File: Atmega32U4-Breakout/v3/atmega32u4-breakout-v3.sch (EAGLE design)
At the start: 54 parts, among them U1 ATMEGA32U4

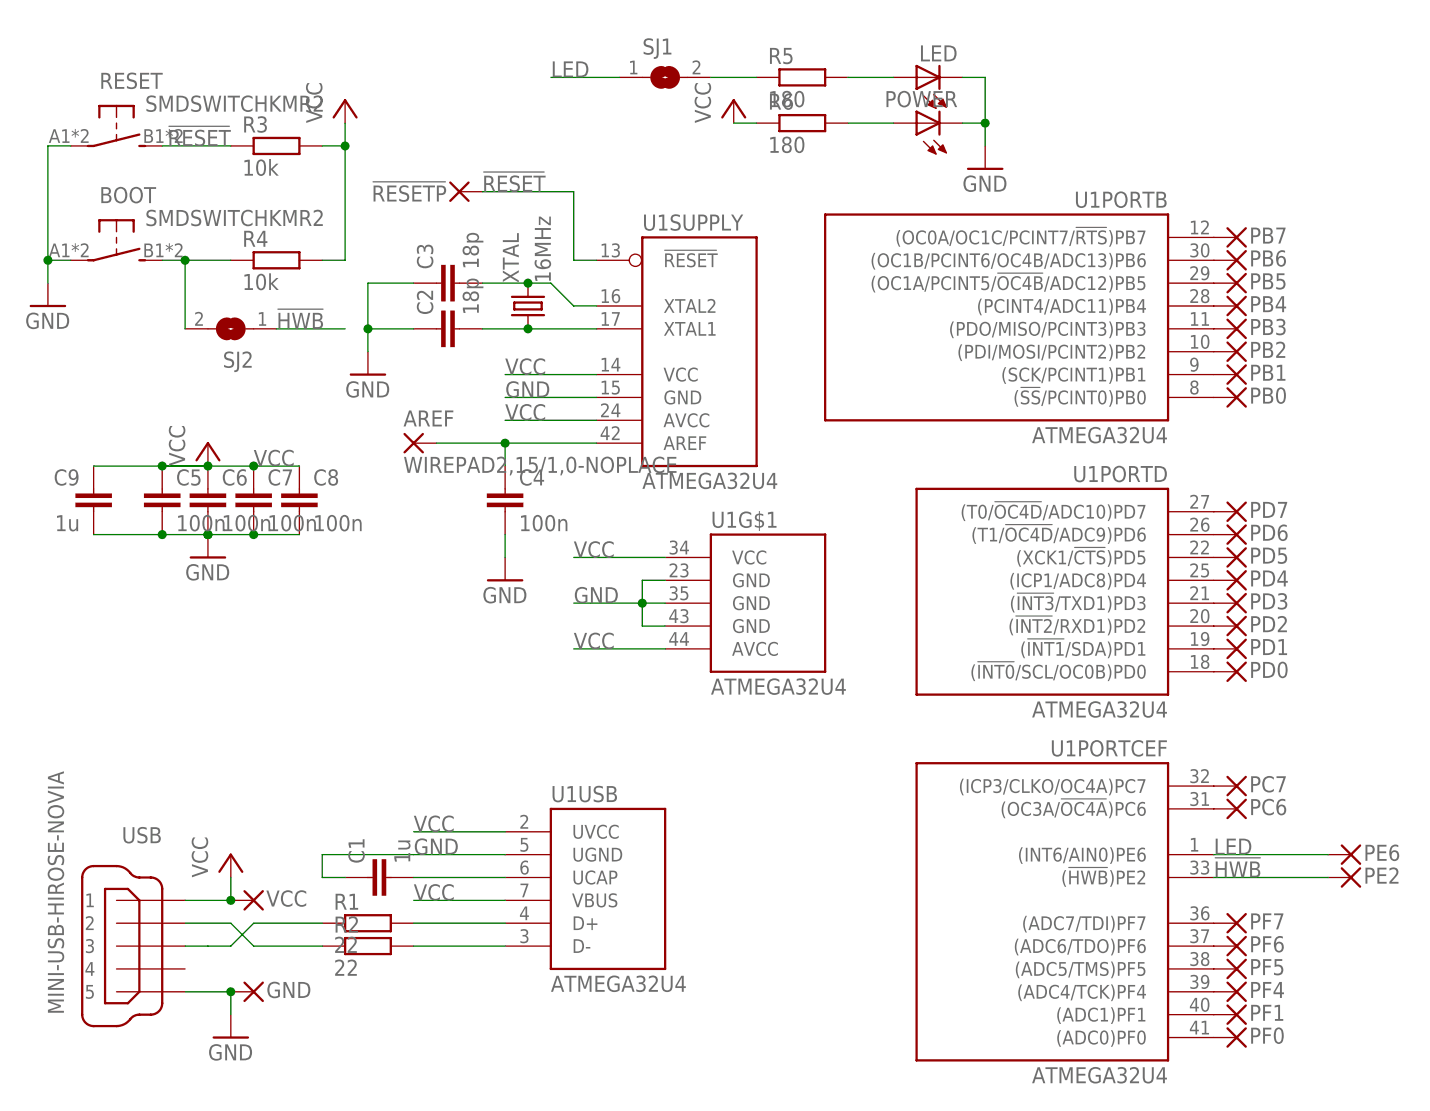
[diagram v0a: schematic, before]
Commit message: - Add silkscreen line between LED resistors so their orientation becomes   more clear. - Change green LED resistor to 150R - Change input filter cap to 0805 4.7uF - Match BOM
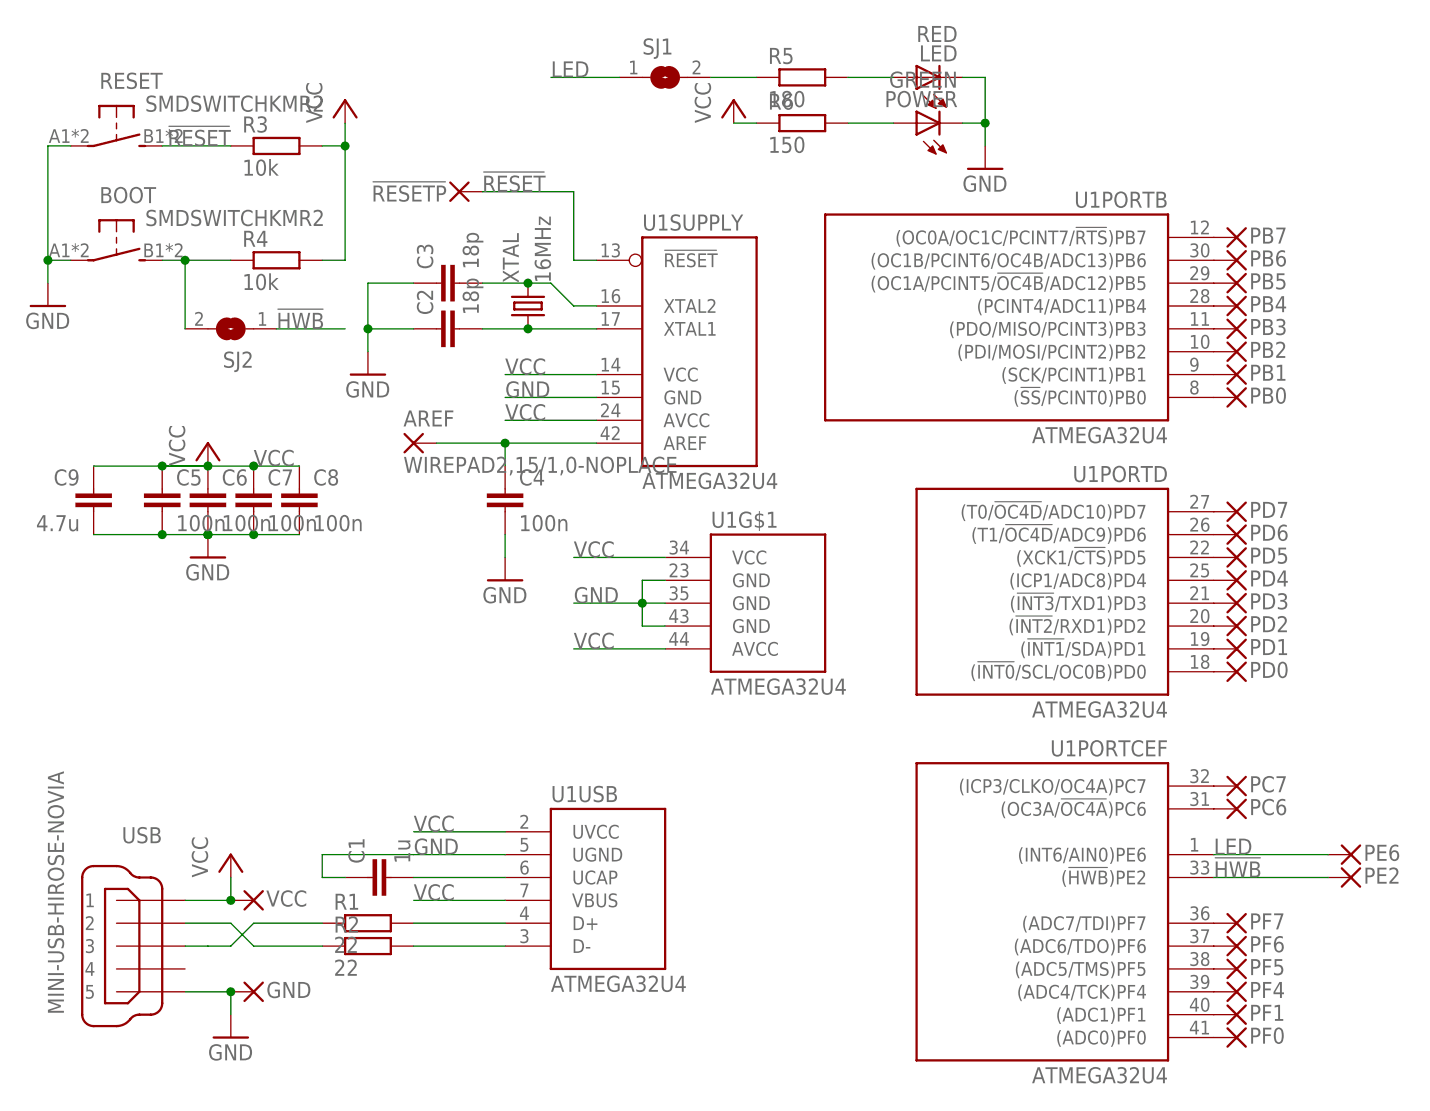
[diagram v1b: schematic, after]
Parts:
- C9: value 1u -> 4.7u; device rcl:C-EUC0603K -> rcl:C-EUC0805K
- LED: value (none) -> RED
- POWER: value (none) -> GREEN
- R6: value 180 -> 150
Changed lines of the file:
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@@
 <?xml version="1.0" encoding="utf-8"?>
 <!DOCTYPE eagle SYSTEM "eagle.dtd">
-<eagle version="6.0">
+<eagle version="6.1">
 <drawing>
 <settings>
@@
 <grid distance="0.1" unitdist="inch" unit="inch" style="lines" multiple="1" display="no" altdistance="0.01" altunitdist="inch" altunit="inch"/>
 <layers>
-<layer number="1" name="Top" color="4" fill="1" visible="yes" active="no"/>
-<layer number="16" name="Bottom" color="1" fill="1" visible="yes" active="no"/>
-<layer number="17" name="Pads" color="2" fill="1" visible="yes" active="no"/>
-<layer number="18" name="Vias" color="2" fill="1" visible="yes" active="no"/>
-<layer number="19" name="Unrouted" color="6" fill="1" visible="yes" active="no"/>
-<layer number="20" name="Dimension" color="15" fill="1" visible="yes" active="no"/>
-<layer number="21" name="tPlace" color="7" fill="1" visible="yes" active="no"/>
-<layer number="22" name="bPlace" color="7" fill="1" visible="yes" active="no"/>
-<layer number="23" name="tOrigins" color="15" fill="1" visible="yes" active="no"/>
-<layer number="24" name="bOrigins" color="15" fill="1" visible="yes" active="no"/>
-<layer number="25" name="tNames" color="7" fill="1" visible="yes" active="no"/>
-<layer number="26" name="bNames" color="7" fill="1" visible="yes" active="no"/>
-<layer number="27" name="tValues" color="7" fill="1" visible="yes" active="no"/>
-<layer number="28" name="bValues" color="7" fill="1" visible="yes" active="no"/>
+<layer number="1" name="Top" color="4" fill="1" visible="no" active="no"/>
+<layer number="16" name="Bottom" color="1" fill="1" visible="no" active="no"/>
+<layer number="17" name="Pads" color="2" fill="1" visible="no" active="no"/>
+<layer number="18" name="Vias" color="2" fill="1" visible="no" active="no"/>
+<layer number="19" name="Unrouted" color="6" fill="1" visible="no" active="no"/>
+<layer number="20" name="Dimension" color="15" fill="1" visible="no" active="no"/>
+<layer number="21" name="tPlace" color="7" fill="1" visible="no" active="no"/>
+<layer number="22" name="bPlace" color="7" fill="1" visible="no" active="no"/>
+<layer number="23" name="tOrigins" color="15" fill="1" visible="no" active="no"/>
+<layer number="24" name="bOrigins" color="15" fill="1" visible="no" active="no"/>
+<layer number="25" name="tNames" color="7" fill="1" visible="no" active="no"/>
+<layer number="26" name="bNames" color="7" fill="1" visible="no" active="no"/>
+<layer number="27" name="tValues" color="7" fill="1" visible="no" active="no"/>
+<layer number="28" name="bValues" color="7" fill="1" visible="no" active="no"/>
 <layer number="29" name="tStop" color="7" fill="3" visible="no" active="no"/>
 <layer number="30" name="bStop" color="7" fill="6" visible="no" active="no"/>
@@
 <layer number="35" name="tGlue" color="7" fill="4" visible="no" active="no"/>
 <layer number="36" name="bGlue" color="7" fill="5" visible="no" active="no"/>
-<layer number="37" name="tTest" color="7" fill="1" visible="yes" active="no"/>
-<layer number="38" name="bTest" color="7" fill="1" visible="yes" active="no"/>
+<layer number="37" name="tTest" color="7" fill="1" visible="no" active="no"/>
+<layer number="38" name="bTest" color="7" fill="1" visible="no" active="no"/>
 <layer number="39" name="tKeepout" color="4" fill="11" visible="no" active="no"/>
 <layer number="40" name="bKeepout" color="1" fill="11" visible="no" active="no"/>
@@
 <layer number="44" name="Drills" color="7" fill="1" visible="no" active="no"/>
 <layer number="45" name="Holes" color="7" fill="1" visible="no" active="no"/>
-<layer number="46" name="Milling" color="3" fill="1" visible="yes" active="no"/>
-<layer number="47" name="Measures" color="7" fill="1" visible="yes" active="no"/>
-<layer number="48" name="Document" color="7" fill="1" visible="yes" active="no"/>
-<layer number="49" name="Reference" color="7" fill="1" visible="yes" active="no"/>
-<layer number="50" name="dxf" color="7" fill="1" visible="yes" active="no"/>
-<layer number="51" name="tDocu" color="7" fill="1" visible="yes" active="no"/>
-<layer number="52" name="bDocu" color="7" fill="1" visible="yes" active="no"/>
-<layer number="53" name="tGND_GNDA" color="7" fill="9" visible="yes" active="no"/>
-<layer number="54" name="bGND_GNDA" color="1" fill="9" visible="yes" active="no"/>
-<layer number="56" name="wert" color="7" fill="1" visible="yes" active="no"/>
+<layer number="46" name="Milling" color="3" fill="1" visible="no" active="no"/>
+<layer number="47" name="Measures" color="7" fill="1" visible="no" active="no"/>
+<layer number="48" name="Document" color="7" fill="1" visible="no" active="no"/>
+<layer number="49" name="Reference" color="7" fill="1" visible="no" active="no"/>
+<layer number="50" name="dxf" color="7" fill="1" visible="no" active="no"/>
+<layer number="51" name="tDocu" color="7" fill="1" visible="no" active="no"/>
+<layer number="52" name="bDocu" color="7" fill="1" visible="no" active="no"/>
+<layer number="53" name="tGND_GNDA" color="7" fill="9" visible="no" active="no"/>
+<layer number="54" name="bGND_GNDA" color="1" fill="9" visible="no" active="no"/>
+<layer number="56" name="wert" color="7" fill="1" visible="no" active="no"/>
 <layer number="91" name="Nets" color="2" fill="1" visible="yes" active="yes"/>
 <layer number="92" name="Busses" color="1" fill="1" visible="yes" active="yes"/>
@@
 <part name="GND4" library="supply1" deviceset="GND" device=""/>
 <part name="P+2" library="supply1" deviceset="VCC" device=""/>
-<part name="C9" library="rcl" deviceset="C-EU" device="C0603K" value="1u"/>
+<part name="C9" library="rcl" deviceset="C-EU" device="C0805K" value="4.7u"/>
 <part name="PB0" library="jocki" deviceset="WIREPAD" device="2,15/1,0-NOPLACE"/>
 <part name="PB1" library="jocki" deviceset="WIREPAD" device="2,15/1,0-NOPLACE"/>
@@
 <part name="VCC" library="jocki" deviceset="WIREPAD" device="2,15/1,0-NOPLACE"/>
 <part name="R5" library="rcl" deviceset="R-EU_" device="R0603" value="180"/>
-<part name="R6" library="rcl" deviceset="R-EU_" device="R0603" value="180"/>
+<part name="R6" library="rcl" deviceset="R-EU_" device="R0603" value="150"/>
 <part name="SJ1" library="jumper" deviceset="SJ" device=""/>
-<part name="LED" library="led" deviceset="LED" device="CHIPLED_0805"/>
-<part name="POWER" library="led" deviceset="LED" device="CHIPLED_0805"/>
+<part name="LED" library="led" deviceset="LED" device="CHIPLED_0805" value="RED"/>
+<part name="POWER" library="led" deviceset="LED" device="CHIPLED_0805" value="GREEN"/>
 <part name="GND8" library="supply1" deviceset="GND" device=""/>
 <part name="P+4" library="supply1" deviceset="VCC" device=""/>

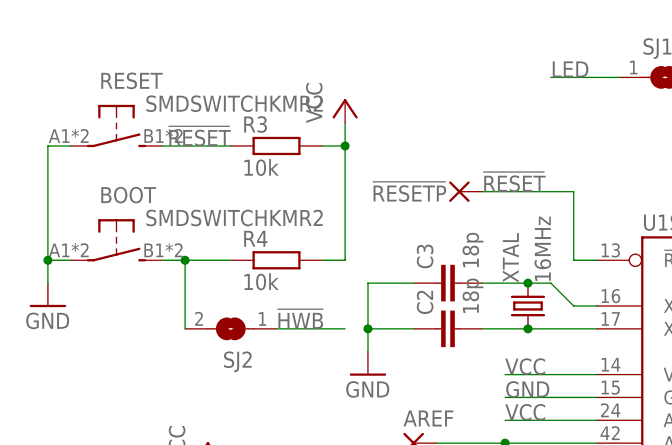
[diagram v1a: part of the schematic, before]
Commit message: Straighten a few bits of the layout, adapt to switches with ground pin. Also, match BOM.
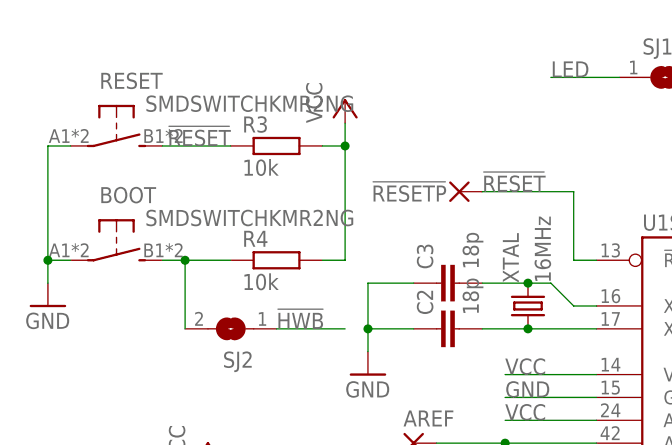
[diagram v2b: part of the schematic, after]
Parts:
- BOOT, RESET: value SMDSWITCHKMR2 -> SMDSWITCHKMR2NG; device jocki:SMDSWITCHKMR2 -> jocki:SMDSWITCHKMR2NG
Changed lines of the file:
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@@
 <grid distance="0.1" unitdist="inch" unit="inch" style="lines" multiple="1" display="no" altdistance="0.01" altunitdist="inch" altunit="inch"/>
 <layers>
-<layer number="1" name="Top" color="4" fill="1" visible="no" active="no"/>
-<layer number="16" name="Bottom" color="1" fill="1" visible="no" active="no"/>
-<layer number="17" name="Pads" color="2" fill="1" visible="no" active="no"/>
-<layer number="18" name="Vias" color="2" fill="1" visible="no" active="no"/>
-<layer number="19" name="Unrouted" color="6" fill="1" visible="no" active="no"/>
-<layer number="20" name="Dimension" color="15" fill="1" visible="no" active="no"/>
-<layer number="21" name="tPlace" color="7" fill="1" visible="no" active="no"/>
-<layer number="22" name="bPlace" color="7" fill="1" visible="no" active="no"/>
-<layer number="23" name="tOrigins" color="15" fill="1" visible="no" active="no"/>
-<layer number="24" name="bOrigins" color="15" fill="1" visible="no" active="no"/>
-<layer number="25" name="tNames" color="7" fill="1" visible="no" active="no"/>
-<layer number="26" name="bNames" color="7" fill="1" visible="no" active="no"/>
-<layer number="27" name="tValues" color="7" fill="1" visible="no" active="no"/>
-<layer number="28" name="bValues" color="7" fill="1" visible="no" active="no"/>
+<layer number="1" name="Top" color="4" fill="1" visible="yes" active="no"/>
+<layer number="16" name="Bottom" color="1" fill="1" visible="yes" active="no"/>
+<layer number="17" name="Pads" color="2" fill="1" visible="yes" active="no"/>
+<layer number="18" name="Vias" color="2" fill="1" visible="yes" active="no"/>
+<layer number="19" name="Unrouted" color="6" fill="1" visible="yes" active="no"/>
+<layer number="20" name="Dimension" color="15" fill="1" visible="yes" active="no"/>
+<layer number="21" name="tPlace" color="7" fill="1" visible="yes" active="no"/>
+<layer number="22" name="bPlace" color="7" fill="1" visible="yes" active="no"/>
+<layer number="23" name="tOrigins" color="15" fill="1" visible="yes" active="no"/>
+<layer number="24" name="bOrigins" color="15" fill="1" visible="yes" active="no"/>
+<layer number="25" name="tNames" color="7" fill="1" visible="yes" active="no"/>
+<layer number="26" name="bNames" color="7" fill="1" visible="yes" active="no"/>
+<layer number="27" name="tValues" color="7" fill="1" visible="yes" active="no"/>
+<layer number="28" name="bValues" color="7" fill="1" visible="yes" active="no"/>
 <layer number="29" name="tStop" color="7" fill="3" visible="no" active="no"/>
 <layer number="30" name="bStop" color="7" fill="6" visible="no" active="no"/>
@@
 <layer number="35" name="tGlue" color="7" fill="4" visible="no" active="no"/>
 <layer number="36" name="bGlue" color="7" fill="5" visible="no" active="no"/>
-<layer number="37" name="tTest" color="7" fill="1" visible="no" active="no"/>
-<layer number="38" name="bTest" color="7" fill="1" visible="no" active="no"/>
+<layer number="37" name="tTest" color="7" fill="1" visible="yes" active="no"/>
+<layer number="38" name="bTest" color="7" fill="1" visible="yes" active="no"/>
 <layer number="39" name="tKeepout" color="4" fill="11" visible="no" active="no"/>
 <layer number="40" name="bKeepout" color="1" fill="11" visible="no" active="no"/>
@@
 <layer number="44" name="Drills" color="7" fill="1" visible="no" active="no"/>
 <layer number="45" name="Holes" color="7" fill="1" visible="no" active="no"/>
-<layer number="46" name="Milling" color="3" fill="1" visible="no" active="no"/>
-<layer number="47" name="Measures" color="7" fill="1" visible="no" active="no"/>
-<layer number="48" name="Document" color="7" fill="1" visible="no" active="no"/>
-<layer number="49" name="Reference" color="7" fill="1" visible="no" active="no"/>
-<layer number="50" name="dxf" color="7" fill="1" visible="no" active="no"/>
-<layer number="51" name="tDocu" color="7" fill="1" visible="no" active="no"/>
-<layer number="52" name="bDocu" color="7" fill="1" visible="no" active="no"/>
-<layer number="53" name="tGND_GNDA" color="7" fill="9" visible="no" active="no"/>
-<layer number="54" name="bGND_GNDA" color="1" fill="9" visible="no" active="no"/>
-<layer number="56" name="wert" color="7" fill="1" visible="no" active="no"/>
+<layer number="46" name="Milling" color="3" fill="1" visible="yes" active="no"/>
+<layer number="47" name="Measures" color="7" fill="1" visible="yes" active="no"/>
+<layer number="48" name="Document" color="7" fill="1" visible="yes" active="no"/>
+<layer number="49" name="Reference" color="7" fill="1" visible="yes" active="no"/>
+<layer number="50" name="dxf" color="7" fill="1" visible="yes" active="no"/>
+<layer number="51" name="tDocu" color="7" fill="1" visible="yes" active="no"/>
+<layer number="52" name="bDocu" color="7" fill="1" visible="yes" active="no"/>
+<layer number="53" name="tGND_GNDA" color="7" fill="9" visible="yes" active="no"/>
+<layer number="54" name="bGND_GNDA" color="1" fill="9" visible="yes" active="no"/>
+<layer number="56" name="wert" color="7" fill="1" visible="yes" active="no"/>
 <layer number="91" name="Nets" color="2" fill="1" visible="yes" active="yes"/>
 <layer number="92" name="Busses" color="1" fill="1" visible="yes" active="yes"/>
@@
 <part name="R3" library="rcl" deviceset="R-EU_" device="R0603" value="10k"/>
 <part name="P+3" library="supply1" deviceset="VCC" device=""/>
-<part name="RESET" library="jocki" deviceset="SMDSWITCH" device="KMR2"/>
+<part name="RESET" library="jocki" deviceset="SMDSWITCH" device="KMR2NG"/>
 <part name="GND" library="jocki" deviceset="WIREPAD" device="2,15/1,0-NOPLACE"/>
 <part name="VCC" library="jocki" deviceset="WIREPAD" device="2,15/1,0-NOPLACE"/>
@@
 <part name="P+4" library="supply1" deviceset="VCC" device=""/>
 <part name="GND5" library="supply1" deviceset="GND" device=""/>
-<part name="BOOT" library="jocki" deviceset="SMDSWITCH" device="KMR2"/>
+<part name="BOOT" library="jocki" deviceset="SMDSWITCH" device="KMR2NG"/>
 <part name="R4" library="rcl" deviceset="R-EU_" device="R0603" value="10k"/>
 <part name="!RESETP" library="jocki" deviceset="WIREPAD" device="2,15/1,0-NOPLACE"/>
